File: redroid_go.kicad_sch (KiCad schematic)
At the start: 95 parts, among them J1 USB4105-GF-A, J2 5051101892, J3 Conn_01x02_Pin, J4 Conn_01x10_Pin, Q1 UMH3N, Q2 PMOS, Q3 UMH3N, SW1 UP, SW10 A, SW11 SW_SPDT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

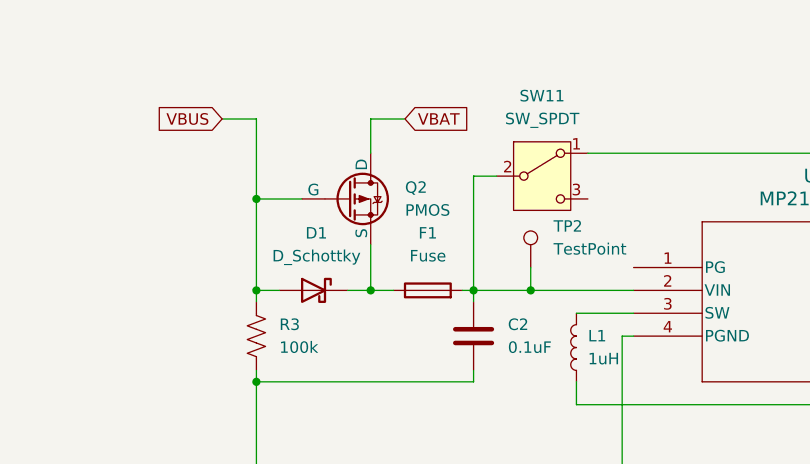
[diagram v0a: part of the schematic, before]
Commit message: Fix battery/VBUS PMOS polarity
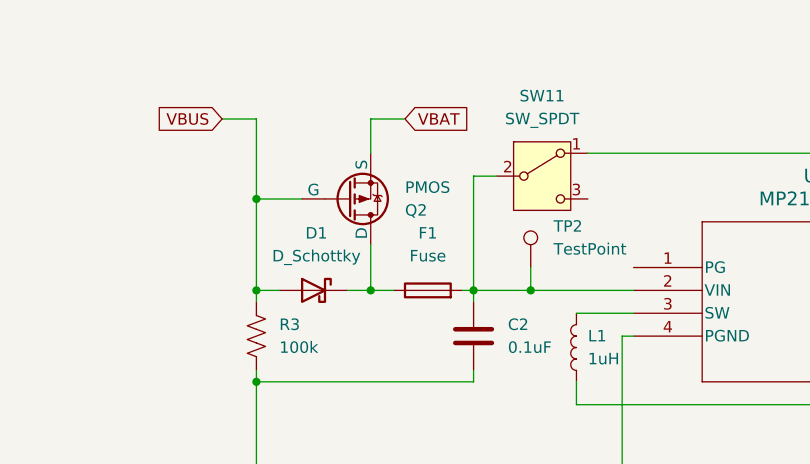
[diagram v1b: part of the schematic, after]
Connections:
- net VBAT: now also Q2.3 (S); no longer Q2.1 (D)
- net at D1.1 (K), F1.1: now also Q2.1 (D); no longer Q2.3 (S)
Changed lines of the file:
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@@
 	)
 	(junction
+		(at 279.4 45.72)
+		(diameter 0)
+		(color 0 0 0 0)
+	)
+	(junction
 		(at 330.2 71.12)
 		(diameter 0)
@@
 	)
 	(junction
-		(at 279.4 45.72)
-		(diameter 0)
-		(color 0 0 0 0)
-	)
-	(junction
 		(at 66.04 144.78)
 		(diameter 0)
@@
 	(wire
 		(pts
+			(xy 279.4 45.72) (xy 281.94 45.72)
+		)
+		(stroke
+			(width 0)
+			(type default)
+		)
+	)
+	(wire
+		(pts
 			(xy 229.87 177.8) (xy 250.19 177.8)
 		)
@@
 	(wire
 		(pts
-			(xy 279.4 40.64) (xy 279.4 45.72)
-		)
-		(stroke
-			(width 0)
-			(type default)
-		)
-	)
-	(wire
-		(pts
 			(xy 234.95 175.26) (xy 250.19 175.26)
 		)
@@
 	(wire
 		(pts
-			(xy 279.4 45.72) (xy 281.94 45.72)
+			(xy 276.86 45.72) (xy 279.4 45.72)
 		)
 		(stroke
@@
 	(wire
 		(pts
+			(xy 279.4 26.67) (xy 279.4 30.48)
+		)
+		(stroke
+			(width 0)
+			(type default)
+		)
+	)
+	(wire
+		(pts
 			(xy 246.38 228.6) (xy 251.46 228.6)
 		)
@@
 	(wire
 		(pts
-			(xy 276.86 45.72) (xy 279.4 45.72)
-		)
-		(stroke
-			(width 0)
-			(type default)
-		)
-	)
-	(wire
-		(pts
 			(xy 313.69 172.72) (xy 325.12 172.72)
 		)
@@
 	(wire
 		(pts
+			(xy 279.4 40.64) (xy 279.4 45.72)
+		)
+		(stroke
+			(width 0)
+			(type default)
+		)
+	)
+	(wire
+		(pts
 			(xy 314.96 181.61) (xy 313.69 181.61)
 		)
@@
 	(wire
 		(pts
-			(xy 279.4 30.48) (xy 279.4 26.67)
-		)
-		(stroke
-			(width 0)
-			(type default)
-		)
-	)
-	(wire
-		(pts
 			(xy 356.87 60.96) (xy 359.41 60.96)
 		)
@@
 		(lib_id "Simulation_SPICE:PMOS")
 		(at 276.86 35.56 0)
+		(mirror x)
 		(unit 1)
 		(exclude_from_sim no)
@@
 		(on_board yes)
 		(dnp no)
-		(fields_autoplaced yes)
 		(property "Reference" "Q2"
-			(at 283.21 34.2899 0)
+			(at 283.21 36.8301 0)
 			(effects
 				(font
@@
 		)
 		(property "Value" "PMOS"
-			(at 283.21 36.8299 0)
+			(at 283.21 34.2901 0)
 			(effects
 				(font
@@
 		)
 		(property "Footprint" "Package_TO_SOT_SMD:SOT-23"
-			(at 281.94 33.02 0)
+			(at 281.94 38.1 0)
 			(effects
 				(font
@@
 		)
 		(property "Datasheet" "https://ngspice.sourceforge.io/docs/ngspice-html-manual/manual.xhtml#cha_MOSFETs"
-			(at 276.86 48.26 0)
+			(at 276.86 22.86 0)
 			(effects
 				(font
@@
 		)
 		(property "Sim.Device" "PMOS"
-			(at 276.86 52.705 0)
+			(at 276.86 18.415 0)
 			(effects
 				(font
@@
 		)
 		(property "Sim.Type" "VDMOS"
-			(at 276.86 54.61 0)
+			(at 276.86 16.51 0)
 			(effects
 				(font
@@
 		)
 		(property "Sim.Pins" "1=D 2=G 3=S"
-			(at 276.86 50.8 0)
+			(at 276.86 20.32 0)
 			(effects
 				(font

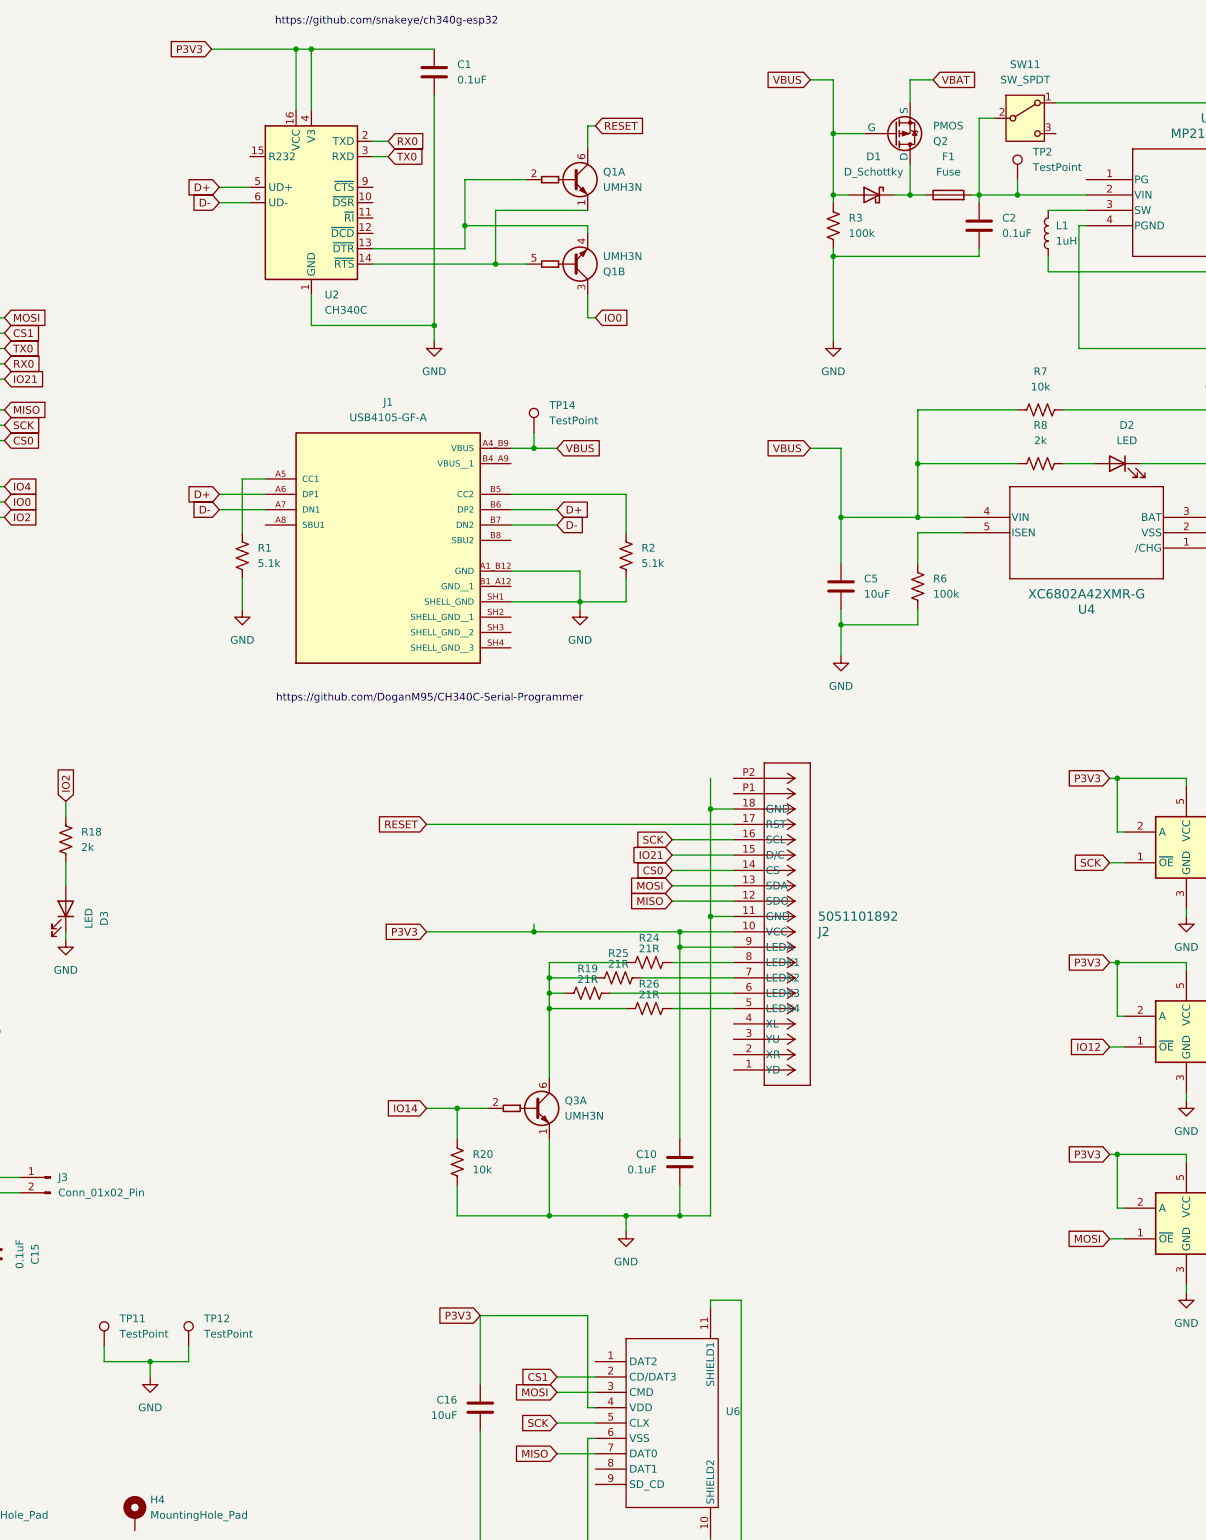
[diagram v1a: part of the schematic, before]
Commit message: Add separate power for serial chip
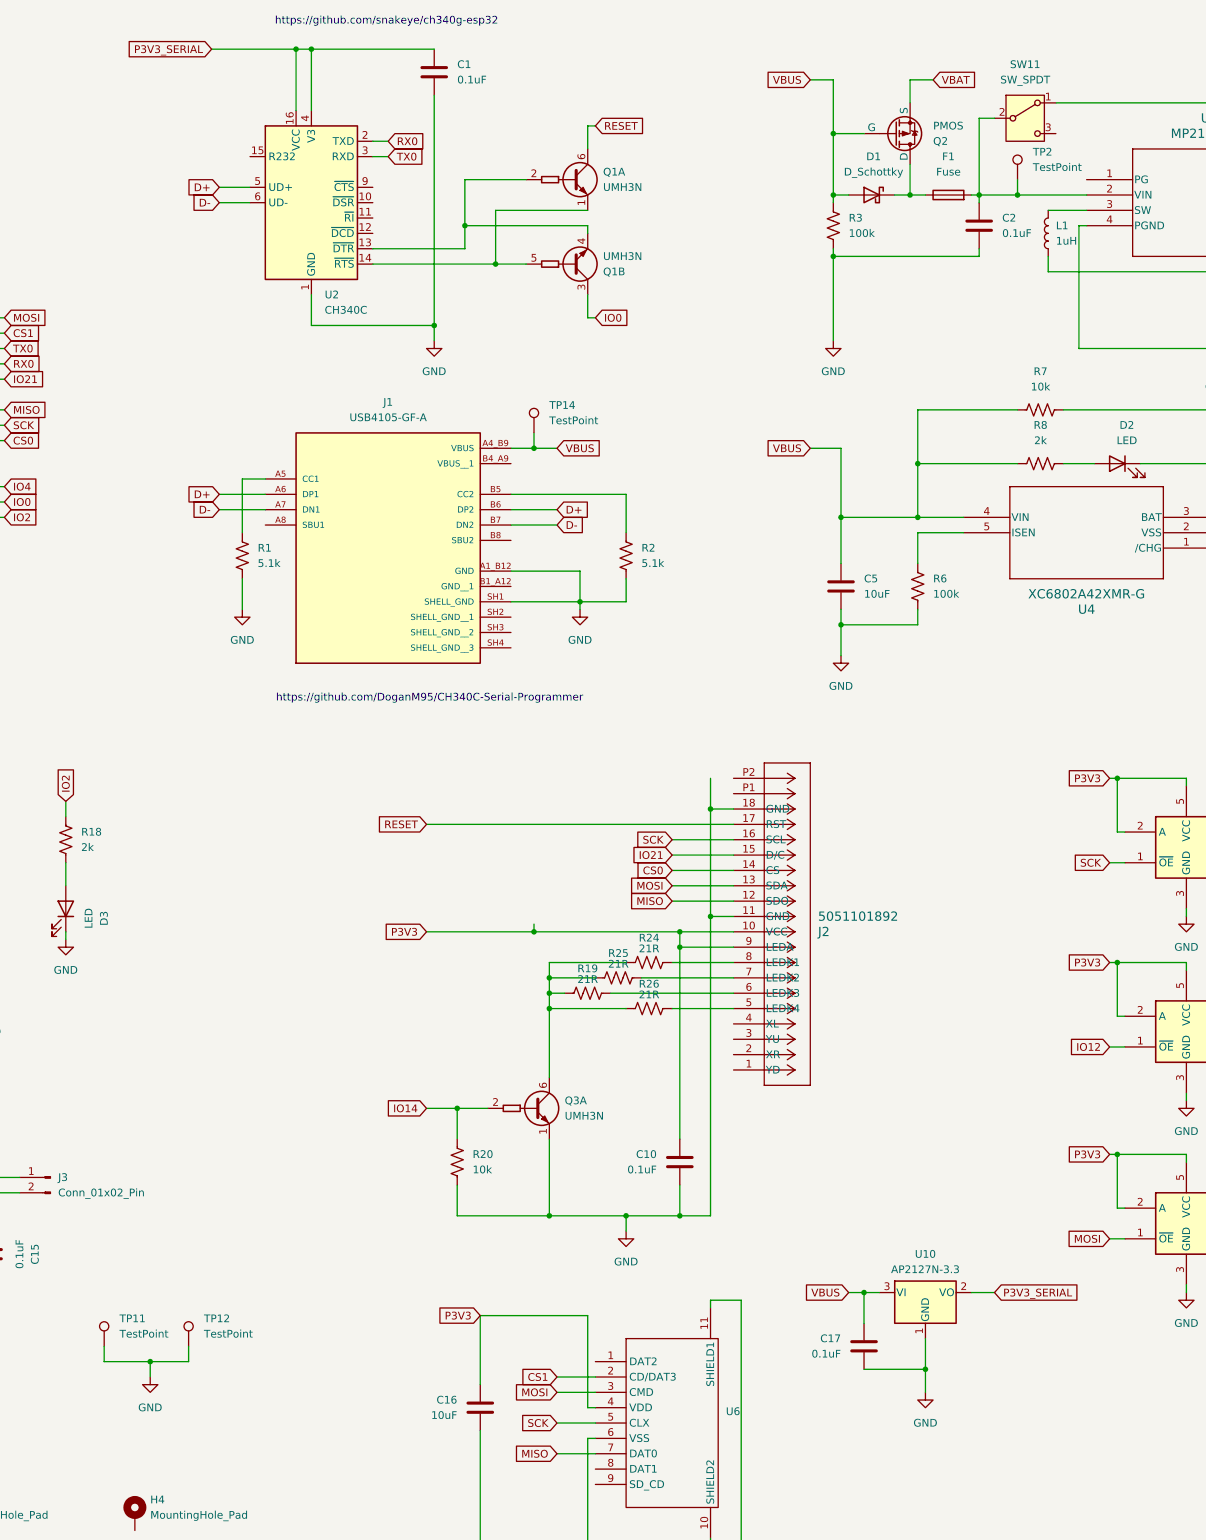
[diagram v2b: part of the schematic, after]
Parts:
- added C17: 0.1uF, Capacitor_SMD:C_0603_1608Metric_Pad1.08x0.95mm_HandSolder, symbol Device:C
- added U10: AP2127N-3.3, Package_TO_SOT_SMD:SOT-23-3, symbol Regulator_Linear:AP2127N-3.3
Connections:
- net GND: now also C17.2, U10.1 (GND)
- net P3V3: no longer C1.1, U2.16 (VCC), U2.4 (V3)
- net VBUS: now also C17.1, U10.3 (VI)
- new net P3V3_SERIAL: C1.1, U10.2 (VO), U2.16 (VCC), U2.4 (V3)

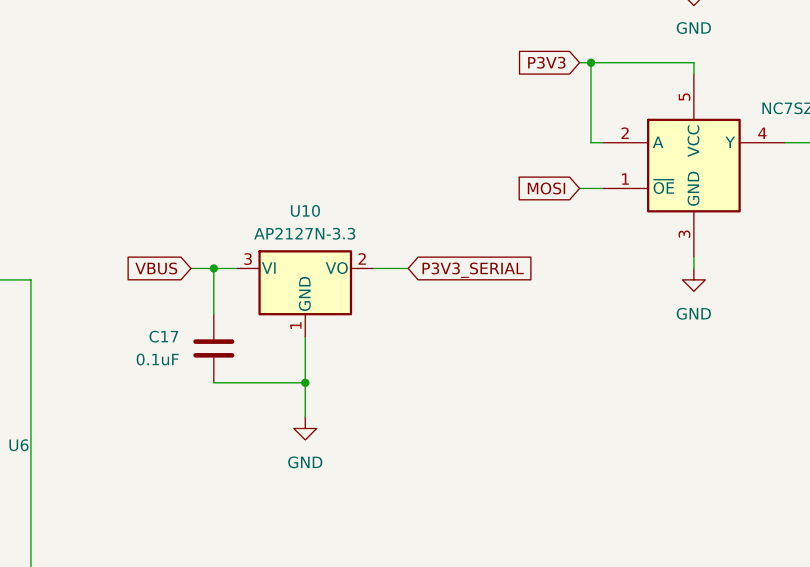
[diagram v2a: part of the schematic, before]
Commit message: Change 3v3 LDO to AMS1117 and add test point
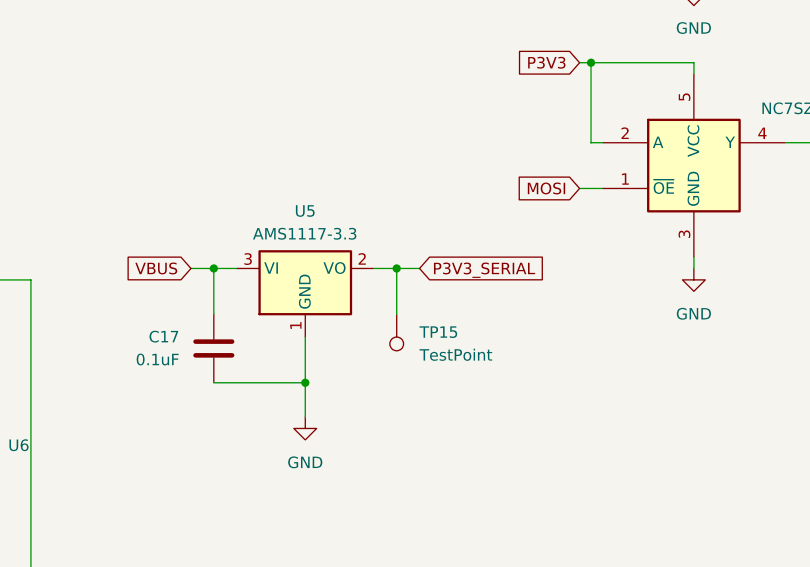
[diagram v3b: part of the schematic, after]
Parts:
- removed U10: AP2127N-3.3, Package_TO_SOT_SMD:SOT-23-3, symbol Regulator_Linear:AP2127N-3.3
- added TP15: TestPoint, TestPoint:TestPoint_Pad_D1.5mm, symbol Connector:TestPoint
- added U5: AMS1117-3.3, Package_TO_SOT_SMD:SOT-223-3_TabPin2, symbol Regulator_Linear:AMS1117-3.3
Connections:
- net GND: now also U5.1 (GND)
- net P3V3_SERIAL: now also TP15.1, U5.2 (VO)
- net VBUS: now also U5.3 (VI)
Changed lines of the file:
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@@
 	)
 	(junction
+		(at 292.1 227.33)
+		(diameter 0)
+		(color 0 0 0 0)
+	)
+	(junction
 		(at 127 208.28)
 		(diameter 0)
@@
 	(wire
 		(pts
-			(xy 289.56 227.33) (xy 293.37 227.33)
+			(xy 289.56 227.33) (xy 292.1 227.33)
 		)
 		(stroke
@@
 	(wire
 		(pts
+			(xy 292.1 227.33) (xy 292.1 232.41)
+		)
+		(stroke
+			(width 0)
+			(type default)
+		)
+	)
+	(wire
+		(pts
 			(xy 139.7 156.21) (xy 139.7 160.02)
 		)
@@
 	(wire
 		(pts
+			(xy 292.1 227.33) (xy 294.64 227.33)
+		)
+		(stroke
+			(width 0)
+			(type default)
+		)
+	)
+	(wire
+		(pts
 			(xy 288.29 101.6) (xy 280.67 101.6)
 		)
@@
 	(global_label "P3V3_SERIAL"
 		(shape input)
-		(at 293.37 227.33 0)
+		(at 294.64 227.33 0)
 		(fields_autoplaced yes)
 		(effects
@@
 		)
 		(property "Intersheetrefs" "${INTERSHEET_REFS}"
-			(at 308.4504 227.33 0)
+			(at 309.7204 227.33 0)
 			(effects
 				(font
@@
 	)
 	(symbol
+		(lib_id "Connector:TestPoint")
+		(at 292.1 232.41 180)
+		(unit 1)
+		(exclude_from_sim no)
+		(in_bom yes)
+		(on_board yes)
+		(dnp no)
+		(fields_autoplaced yes)
+		(property "Reference" "TP15"
+			(at 294.64 234.4419 0)
+			(effects
+				(font
+					(size 1.27 1.27)
+				)
+				(justify right)
+			)
+		)
+		(property "Value" "TestPoint"
+			(at 294.64 236.9819 0)
+			(effects
+				(font
+					(size 1.27 1.27)
+				)
+				(justify right)
+			)
+		)
+		(property "Footprint" "TestPoint:TestPoint_Pad_D1.5mm"
+			(at 287.02 232.41 0)
+			(effects
+				(font
+					(size 1.27 1.27)
+				)
+				(hide yes)
+			)
+		)
+		(property "Datasheet" "~"
+			(at 287.02 232.41 0)
+			(effects
+				(font
+					(size 1.27 1.27)
+				)
+				(hide yes)
+			)
+		)
+		(property "Description" "test point"
+			(at 292.1 232.41 0)
+			(effects
+				(font
+					(size 1.27 1.27)
+				)
+				(hide yes)
+			)
+		)
+		(pin "1"
+		)
+		(instances
+			(project "redroid_go"
+				(path "/54323edd-924e-4c99-bcbf-5375689f8e73"
+					(reference "TP15")
+					(unit 1)
+				)
+			)
+		)
+	)
+	(symbol
 		(lib_id "74xGxx:NC7SZ125M5X")
 		(at 325.12 153.67 0)
@@
 	)
 	(symbol
-		(lib_id "Regulator_Linear:AP2127N-3.3")
-		(at 281.94 227.33 0)
+		(lib_id "32teeth - Conductive Buttons:CONDUCTIVE_BUTTONCONDUCTIVE_BUTTON_THICK")
+		(at 46.99 144.78 0)
+		(mirror y)
 		(unit 1)
 		(exclude_from_sim no)
@@
 		(on_board yes)
 		(dnp no)
-		(fields_autoplaced yes)
-		(property "Reference" "U10"
-			(at 281.94 220.98 0)
+		(property "Reference" "SW2"
+			(at 46.99 140.97 0)
 			(effects
 				(font
-					(size 1.27 1.27)
+					(size 1.9304 1.9304)
+					(thickness 0.3861)
+					(bold yes)
 				)
+				(hide yes)
 			)
 		)
-		(property "Value" "AP2127N-3.3"
-			(at 281.94 223.52 0)
+		(property "Value" "DOWN"
+			(at 46.99 144.78 0)
 			(effects
 				(font
 					(size 1.27 1.27)
 				)
+				(hide yes)
 			)
 		)
-		(property "Footprint" "Package_TO_SOT_SMD:SOT-23-3"
-			(at 281.94 221.615 0)
+		(property "Footprint" "Conductive Button:CONDUCTIVE_BUTTON_DIRECTIONAL_THICK"
+			(at 46.99 144.78 0)
 			(effects
 				(font
 					(size 1.27 1.27)
-					(italic yes)
 				)
 				(hide yes)
 			)
 		)
-		(property "Datasheet" "https://www.diodes.com/assets/Datasheets/AP2127.pdf"
-			(at 281.94 227.33 0)
+		(property "Datasheet" ""
+			(at 46.99 144.78 0)
 			(effects
 				(font
@@
 			)
 		)
-		(property "Description" "300mA low dropout linear regulator, shutdown pin, 2.5V-6V input voltage, 3.3V fixed positive output, SOT-23 package"
-			(at 281.94 227.33 0)
+		(property "Description" "JOY_DOWN"
+			(at 46.99 144.78 0)
 			(effects
 				(font
@@
 			)
 		)
-		(pin "1"
-		)
-		(pin "2"
+		(pin "P$ACTIVE"
 		)
-		(pin "3"
+		(pin "P$GND"
 		)
 		(instances
-			(project ""
+			(project "redroid_go"
 				(path "/54323edd-924e-4c99-bcbf-5375689f8e73"
-					(reference "U10")
+					(reference "SW2")
 					(unit 1)
 				)
@@
 	)
 	(symbol
-		(lib_id "32teeth - Conductive Buttons:CONDUCTIVE_BUTTONCONDUCTIVE_BUTTON_THICK")
-		(at 46.99 144.78 0)
-		(mirror y)
+		(lib_id "Connector:TestPoint")
+		(at 96.52 139.7 0)
+		(mirror x)
 		(unit 1)
 		(exclude_from_sim no)
@@
 		(on_board yes)
 		(dnp no)
-		(property "Reference" "SW2"
-			(at 46.99 140.97 0)
+		(property "Reference" "TP3"
+			(at 99.06 144.2721 0)
 			(effects
 				(font
-					(size 1.9304 1.9304)
-					(thickness 0.3861)
-					(bold yes)
+					(size 1.27 1.27)
 				)
-				(hide yes)
+				(justify left)
 			)
 		)
-		(property "Value" "DOWN"
-			(at 46.99 144.78 0)
+		(property "Value" "TestPoint"
+			(at 99.06 141.7321 0)
 			(effects
 				(font
 					(size 1.27 1.27)
 				)
-				(hide yes)
+				(justify left)
 			)
 		)
-		(property "Footprint" "Conductive Button:CONDUCTIVE_BUTTON_DIRECTIONAL_THICK"
-			(at 46.99 144.78 0)
+		(property "Footprint" "TestPoint:TestPoint_Pad_D1.5mm"
+			(at 101.6 139.7 0)
 			(effects
 				(font
@@
 			)
 		)
-		(property "Datasheet" ""
-			(at 46.99 144.78 0)
+		(property "Datasheet" "~"
+			(at 101.6 139.7 0)
 			(effects
 				(font
@@
 			)
 		)
-		(property "Description" "JOY_DOWN"
-			(at 46.99 144.78 0)
+		(property "Description" "test point"
+			(at 96.52 139.7 0)
 			(effects
 				(font
@@
 			)
 		)
-		(pin "P$ACTIVE"
-		)
-		(pin "P$GND"
+		(pin "1"
 		)
 		(instances
 			(project "redroid_go"
 				(path "/54323edd-924e-4c99-bcbf-5375689f8e73"
-					(reference "SW2")
+					(reference "TP3")
 					(unit 1)
 				)
@@
 	)
 	(symbol
-		(lib_id "Connector:TestPoint")
-		(at 96.52 139.7 0)
-		(mirror x)
+		(lib_id "Regulator_Linear:AMS1117-3.3")
+		(at 281.94 227.33 0)
 		(unit 1)
 		(exclude_from_sim no)
@@
 		(on_board yes)
 		(dnp no)
-		(property "Reference" "TP3"
-			(at 99.06 144.2721 0)
+		(fields_autoplaced yes)
+		(property "Reference" "U5"
+			(at 281.94 220.98 0)
 			(effects
 				(font
 					(size 1.27 1.27)
 				)
-				(justify left)
 			)
 		)
-		(property "Value" "TestPoint"
-			(at 99.06 141.7321 0)
+		(property "Value" "AMS1117-3.3"
+			(at 281.94 223.52 0)
 			(effects
 				(font
 					(size 1.27 1.27)
 				)
-				(justify left)
 			)
 		)
-		(property "Footprint" "TestPoint:TestPoint_Pad_D1.5mm"
-			(at 101.6 139.7 0)
+		(property "Footprint" "Package_TO_SOT_SMD:SOT-223-3_TabPin2"
+			(at 281.94 222.25 0)
 			(effects
 				(font
@@
 			)
 		)
-		(property "Datasheet" "~"
-			(at 101.6 139.7 0)
+		(property "Datasheet" "http://www.advanced-monolithic.com/pdf/ds1117.pdf"
+			(at 284.48 233.68 0)
 			(effects
 				(font
@@
 			)
 		)
-		(property "Description" "test point"
-			(at 96.52 139.7 0)
+		(property "Description" "1A Low Dropout regulator, positive, 3.3V fixed output, SOT-223"
+			(at 281.94 227.33 0)
 			(effects
 				(font
@@
 			)
 		)
+		(pin "3"
+		)
+		(pin "2"
+		)
 		(pin "1"
 		)
 		(instances
-			(project "redroid_go"
+			(project ""
 				(path "/54323edd-924e-4c99-bcbf-5375689f8e73"
-					(reference "TP3")
+					(reference "U5")
 					(unit 1)
 				)
